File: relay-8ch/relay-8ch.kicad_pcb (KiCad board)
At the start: 2 copper layers, 160 x 100 mm, 49 parts, among them J101 Screw_Terminal_01x16, J201 Backplane, K101 FINDER-40.31, K102 FINDER-40.31, K103 FINDER-40.31, K104 FINDER-40.31, K105 FINDER-40.31, K106 FINDER-40.31, K107 FINDER-40.31, K108 FINDER-40.31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

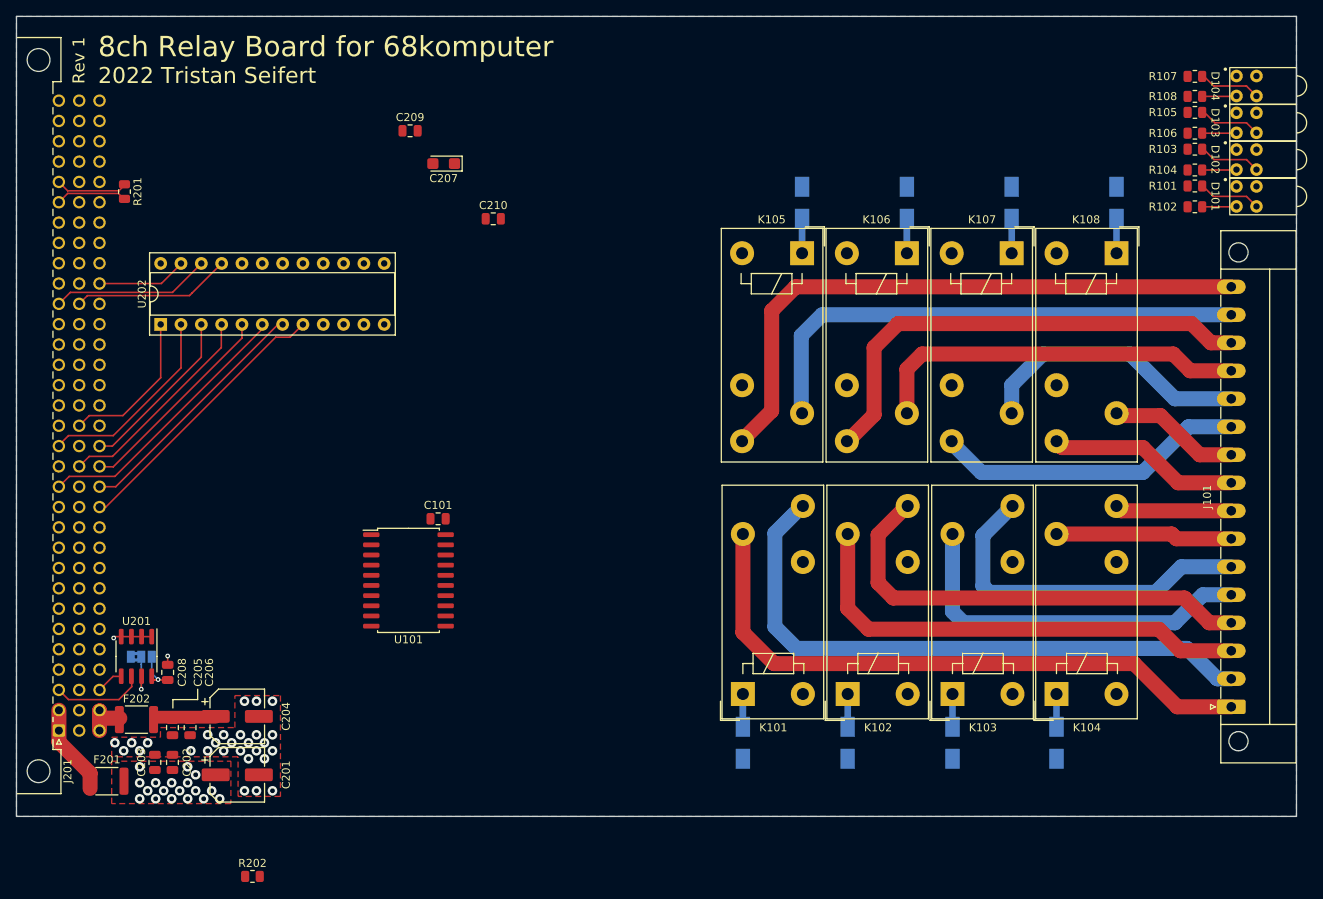
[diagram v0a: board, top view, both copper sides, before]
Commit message: Finished routing relay board
- Completed routing of the relay board; it's got added an address
  selector switch and an I2C expander that can be used to set the
  address automatically.

- Minor tweaks to a few footprints, namely to make sure they're
  correctly tagged as through hole/SMD
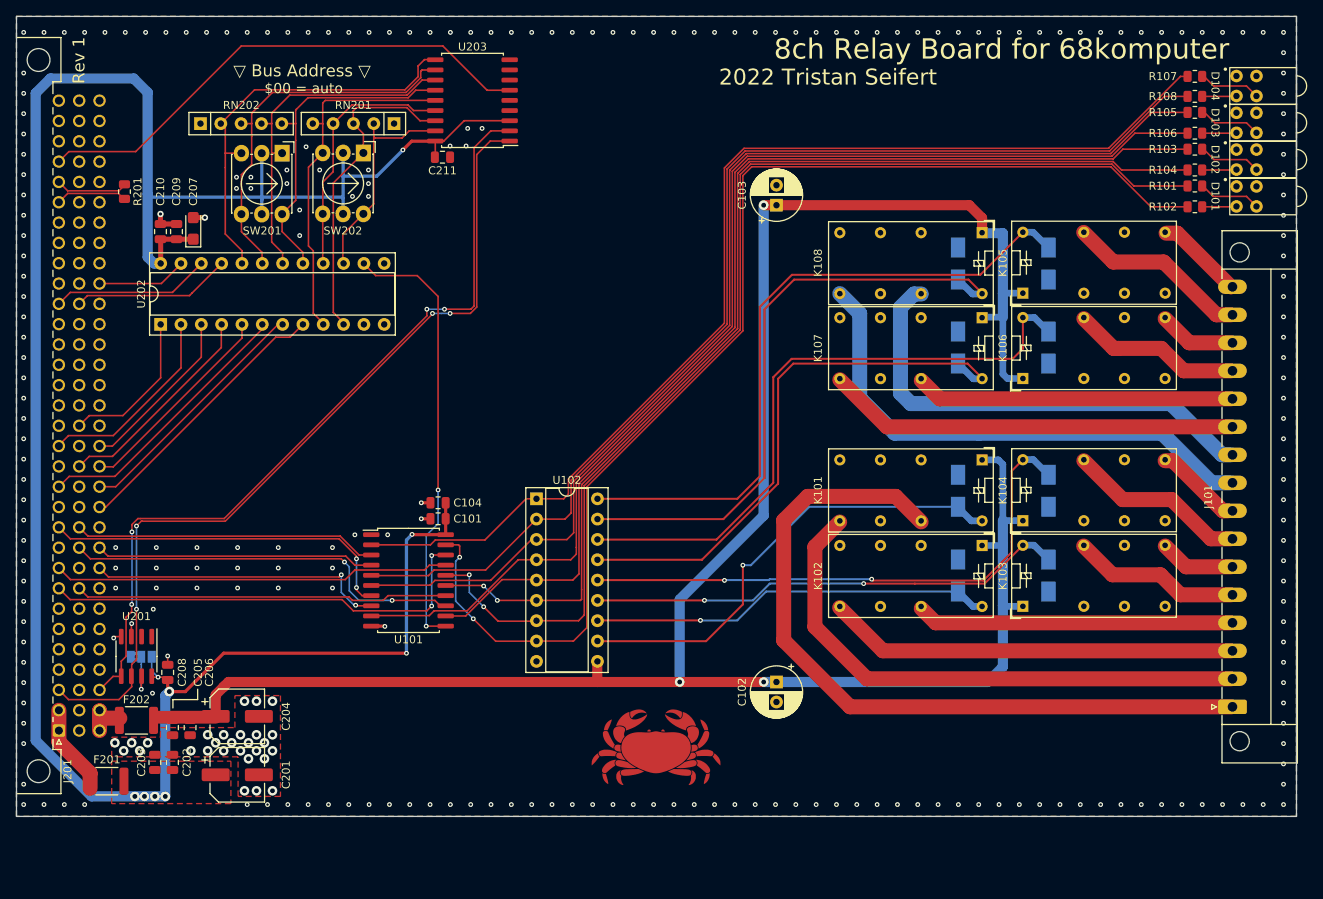
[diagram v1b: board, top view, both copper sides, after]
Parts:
- removed R202: 10k, Resistor_SMD:R_0805_2012Metric
- added C102: 22µF, Capacitor_THT:CP_Radial_D6.3mm_P2.50mm, F.Cu at (115.0, 103.2)
- added C103: 22µF, Capacitor_THT:CP_Radial_D6.3mm_P2.50mm, F.Cu at (115.0, 43.6)
- added C104: 4.7µF, Capacitor_SMD:C_0805_2012Metric, F.Cu at (72.7, 80.8)
- added C211: 100nF, Capacitor_SMD:C_0805_2012Metric, F.Cu at (73.2, 37.6)
- added G***: LOGO, LOGO, F.Cu at (100.0, 111.5)
- added RN201: 10k, Resistor_THT:R_Array_SIP5, F.Cu at (67.2, 33.4)
- added RN202: 10k, Resistor_THT:R_Array_SIP5, F.Cu at (43.0, 33.4)
- added SW201: SW_Coded_SH-7050, Button_Switch_THT:Nidec_Copal_SH-7010C, F.Cu at (53.2, 37.1)
- added SW202: SW_Coded_SH-7050, Button_Switch_THT:Nidec_Copal_SH-7010C, F.Cu at (63.4, 37.1)
- added U102: ULN2803A, Package_DIP:DIP-18_W7.62mm_Socket, F.Cu at (85.0, 80.3)
- added U203: MCP23008-xSO, Package_SO:SOIC-18W_7.5x11.6mm_P1.27mm, F.Cu at (77.0, 30.5)
- K101, K102, K103, K104, K105, K106, K107, K108: value FINDER-40.31 -> G5V-2; footprint Relay_THT:Relay_SPDT_Finder_40.31 -> Relay_THT:Relay_DPDT_Omron_G5V-2
- moved K101 41.8 mm to (140.7, 75.4), turned to -90 degrees
- moved C210 41.6 mm to (38.0, 46.9), turned to 90 degrees
- moved D106 41.4 mm to (137.7, 79.3)
- moved C207 32.3 mm to (42.1, 46.5), turned to 90 degrees
- moved C209 31.8 mm to (40.0, 46.9), turned to 90 degrees
- moved D109 31.7 mm to (149.0, 50.9)
- moved D108 31.5 mm to (149.0, 79.3), turned to 90 degrees
- moved K105 28.0 mm to (145.8, 54.6), turned to 90 degrees
- moved D110 25.3 mm to (149.0, 61.4)
- moved D105 25.0 mm to (137.7, 89.9)
- moved K102 25.0 mm to (140.7, 86.1), turned to -90 degrees
- moved D107 24.1 mm to (149.0, 89.9), turned to 90 degrees
- moved K104 22.1 mm to (145.8, 83.0)
- moved K106 21.3 mm to (145.8, 65.3), turned to 90 degrees
- moved D112 21.2 mm to (137.7, 50.9), turned to -90 degrees
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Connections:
- D105 pad 1: Net-(K102-PadA1) -> GND
- D105 pad 2: GND -> /RELAY1
- D106 pad 1: Net-(K101-PadA1) -> GND
- D106 pad 2: GND -> /RELAY0
- D107 pad 1: Net-(K103-PadA1) -> GND
- D107 pad 2: GND -> /RELAY2
- D108 pad 1: Net-(K104-PadA1) -> GND
- D108 pad 2: GND -> /RELAY3
- D109 pad 1: Net-(K105-PadA1) -> GND
- D109 pad 2: GND -> /RELAY7
- D110 pad 1: Net-(K106-PadA1) -> GND
- D110 pad 2: GND -> /RELAY5
- D111 pad 1: Net-(K107-PadA1) -> GND
- D111 pad 2: GND -> /RELAY4
- D112 pad 1: Net-(K108-PadA1) -> GND
- D112 pad 2: GND -> /RELAY6
- J101 pad 3: /COMM1 -> /SW1
- J101 pad 4: /SW1 -> /COMM1
- J201 pad a11: /Backplane Connection/D2 -> /D2
- J201 pad a8: /Backplane Connection/D7 -> /D7
- J201 pad a9: /Backplane Connection/D6 -> /D6
- J201 pad b10: /Backplane Connection/D4 -> /D4
- J201 pad b11: /Backplane Connection/D0 -> /D0
- J201 pad b8: /Backplane Connection/D5 -> /D5
- J201 pad c10: /Backplane Connection/D1 -> /D1
- J201 pad c9: /Backplane Connection/D3 -> /D3
- K101 pad 11: /COMM0 -> unconnected-(K101-Pad11)
- K102 pad 11: /COMM1 -> unconnected-(K102-Pad11)
- K103 pad 11: /COMM2 -> unconnected-(K103-Pad11)
- K104 pad 11: /COMM3 -> unconnected-(K104-Pad11)
- K105 pad 11: /COMM7 -> unconnected-(K105-Pad11)
- K106 pad 11: /COMM6 -> unconnected-(K106-Pad11)
- K107 pad 11: /COMM5 -> unconnected-(K107-Pad11)
- K108 pad 11: /COMM4 -> unconnected-(K108-Pad11)
- R101 pad 2: unconnected-(R101-Pad2) -> /OUT6
- R102 pad 2: unconnected-(R102-Pad2) -> /OUT7
- R103 pad 2: unconnected-(R103-Pad2) -> /OUT4
- R104 pad 2: unconnected-(R104-Pad2) -> /OUT5
- R105 pad 2: unconnected-(R105-Pad2) -> /OUT2
- R106 pad 2: unconnected-(R106-Pad2) -> /OUT3
- R107 pad 2: unconnected-(R107-Pad2) -> /OUT0
- R108 pad 2: unconnected-(R108-Pad2) -> /OUT1
- U101 pad 12: unconnected-(U101-Pad12) -> /OUT4
- U101 pad 15: unconnected-(U101-Pad15) -> /OUT5
- U101 pad 16: unconnected-(U101-Pad16) -> /OUT6
- U101 pad 19: unconnected-(U101-Pad19) -> /OUT7
- U101 pad 2: unconnected-(U101-Pad2) -> /OUT0
- U101 pad 5: unconnected-(U101-Pad5) -> /OUT1
- U101 pad 6: unconnected-(U101-Pad6) -> /OUT2
- U101 pad 9: unconnected-(U101-Pad9) -> /OUT3
- U202 pad 10: unconnected-(U202-Pad10) -> /Backplane Connection/SET0
- U202 pad 14: /Backplane Connection/LATCH -> /LATCH
- U202 pad 15: unconnected-(U202-Pad15) -> /Backplane Connection/SET3
- U202 pad 16: unconnected-(U202-Pad16) -> /Backplane Connection/SET1
- U202 pad 17: unconnected-(U202-Pad17) -> /Backplane Connection/SET7
- U202 pad 18: unconnected-(U202-Pad18) -> /Backplane Connection/SET4
- U202 pad 19: unconnected-(U202-Pad19) -> /Backplane Connection/SET5
- U202 pad 20: unconnected-(U202-Pad20) -> /Backplane Connection/SET6
- U202 pad 9: unconnected-(U202-Pad9) -> /Backplane Connection/SET2
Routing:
- net +5V: track 5.78 -> 285.8 mm, vias 19 -> 9
- net +12V: track 7.40 -> 270.5 mm, vias 0 -> 3
- net /OUT7: track 0.00 -> 150.9 mm, vias 0 -> 2
- net /OUT3: track 0.00 -> 143.6 mm
- net /OUT6: track 0.00 -> 142.2 mm, vias 0 -> 2
- net /OUT2: track 0.00 -> 141.6 mm
- net /OUT1: track 0.00 -> 140.7 mm
- net /OUT0: track 0.00 -> 138.7 mm
- net /OUT5: track 0.00 -> 136.4 mm, vias 0 -> 2
- net /OUT4: track 0.00 -> 134.9 mm
- net /Backplane Connection/I2C_SDA: track 3.32 -> 102.3 mm, vias 0 -> 4
- net /Backplane Connection/I2C_SCL: track 11.5 -> 108.3 mm, vias 0 -> 4
- net /RELAY7: track 0.00 -> 83.4 mm
- net /RELAY5: track 0.00 -> 78.6 mm
- net /RELAY6: track 0.00 -> 77.3 mm
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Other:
- board text added: "$00 = auto"
- board text added: "▽ Bus Address ▽"

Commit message: Function codes, /DTACK for relay board
- Consider the state of the function code signals (so we don't decode
  CPU space cycles as accesses) and assert /DTACK when the latch signal
  is asserted. This should work for bus speeds of up to around 16MHz
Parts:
- added U204: 74HC00, Package_SO:SOIC-14_3.9x8.7mm_P1.27mm, F.Cu at (40.5, 43.5)
- added U205: 74LVC1G06, 68komputer-common:SC-74-5_1.5x2.9mm_P0.95mm, F.Cu at (34.3, 62.2)
- C207, C209, C210: moved to B.Cu
- moved C207 0.50 mm to (42.1, 47.0)
- moved C209 0.50 mm to (40.0, 47.4)
- moved C210 0.50 mm to (38.0, 47.4)
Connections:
- U202 pad 11: unconnected-(U202-Pad11) -> /Backplane Connection/CPUSPACE
- U202 pad 13: unconnected-(U202-Pad13) -> /Backplane Connection/SET3
- U202 pad 15: /Backplane Connection/SET3 -> unconnected-(U202-Pad15)
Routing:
- net /LATCH: track 55.3 -> 94.8 mm, vias 2 -> 4
- net /Backplane Connection/CPUSPACE: track 0.00 -> 35.8 mm, vias 0 -> 1
- net /Backplane Connection/~{DTACK}: track 0.00 -> 18.8 mm
- net /Backplane Connection/FC1: track 0.00 -> 18.6 mm
- net +5V: track 285.8 -> 301.3 mm, vias 9 -> 11
- net /Backplane Connection/FC0: track 0.00 -> 15.1 mm
- net /Backplane Connection/FC2: track 0.00 -> 9.17 mm
- net GND: track 12.5 -> 7.77 mm, vias 267 -> 291
- net Net-(U204-Pad3): track 0.00 -> 1.28 mm
- net /Backplane Connection/SET3: track 27.2 -> 27.9 mm
- net /SW4: track 64.9 -> 65.5 mm
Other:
- board text added: "0"
- board text added: "1"
- board text added: "1/0"
- board text added: "2"
- board text added: "3"
- board text added: "3/2"
- board text added: "4"
- board text added: "5"
- board text added: "5/4"
- board text added: "6"
- board text added: "7"
- board text added: "7/6"
- board text added: "⚠ 2A/24VDC Max ⚠ ⚠ .6A/115VAC Max ⚠"

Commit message: Tweaks to bill of materials
- Added missing MPN's for a few components; tweaked a few bits of layout
  to increase some tolerances

  This includes kind of tweaking the boot rom socket positions in hopes
  of fitting fancier sockets
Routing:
- net +12V: vias 3 -> 2
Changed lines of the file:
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@@
   (segment (start 44.9 107.5) (end 44.9 104.8) (width 1.27) (layer "F.Cu") (net 3))
   (segment (start 46.5 103.2) (end 92.6 103.2) (width 1.27) (layer "F.Cu") (net 3))
+  (segment (start 92.6 103.2) (end 115 103.2) (width 1.27) (layer "F.Cu") (net 3))
   (segment (start 139.1 43.6) (end 140.7 45.2) (width 1.27) (layer "F.Cu") (net 3))
   (segment (start 44.9 107.6) (end 37.5 107.6) (width 1.6) (layer "F.Cu") (net 3))
-  (segment (start 92.6 103.2) (end 113.4 103.2) (width 1.27) (layer "F.Cu") (net 3))
   (segment (start 44.9 104.8) (end 45.85 103.85) (width 1.27) (layer "F.Cu") (net 3))
   (segment (start 45.85 103.85) (end 46.1 103.6) (width 1.27) (layer "F.Cu") (net 3))
   (segment (start 140.7 45.2) (end 140.7 47) (width 1.27) (layer "F.Cu") (net 3))
   (segment (start 45.85 103.85) (end 46.5 103.2) (width 1.27) (layer "F.Cu") (net 3))
-  (via (at 113.4 103.2) (size 1.2) (drill 0.6) (layers "F.Cu" "B.Cu") (net 3))
   (via (at 102.9 103.2) (size 1.2) (drill 0.6) (layers "F.Cu" "B.Cu") (net 3))
   (via (at 113.4 43.6) (size 1.2) (drill 0.6) (layers "F.Cu" "B.Cu") (net 3))
@@
   (segment (start 143.3 76) (end 143.3 83) (width 0.8382) (layer "B.Cu") (net 3))
   (segment (start 143.8625 65.2625) (end 143.3 64.7) (width 0.8382) (layer "B.Cu") (net 3))
-  (segment (start 113.4 103.2) (end 141.4 103.2) (width 1.27) (layer "B.Cu") (net 3))
-  (segment (start 143.3 101.3) (end 143.3 96.4) (width 1.27) (layer "B.Cu") (net 3))
   (segment (start 143.3 86.1) (end 143.3 93.6) (width 1.27) (layer "B.Cu") (net 3))
   (segment (start 143.3 83) (end 143.3 86.1) (width 1.27) (layer "B.Cu") (net 3))
   (segment (start 145.8 65.2625) (end 143.8625 65.2625) (width 0.8382) (layer "B.Cu") (net 3))
+  (segment (start 115 103.2) (end 141.4 103.2) (width 1.27) (layer "B.Cu") (net 3))
+  (segment (start 143.3 101.3) (end 143.3 93.6) (width 1.27) (layer "B.Cu") (net 3))
   (segment (start 143.3 64.7) (end 143.3 57.6) (width 0.8382) (layer "B.Cu") (net 3))
-  (segment (start 143.3 93.6) (end 143.3 96.4) (width 1.27) (layer "B.Cu") (net 3))
   (segment (start 143.3 57.6) (end 143.3 54.6) (width 1.27) (layer "B.Cu") (net 3))
   (segment (start 140.7 86.1375) (end 143.2625 86.1375) (width 0.8382) (layer "B.Cu") (net 3))
+  (segment (start 141.4 103.2) (end 143.3 101.3) (width 1.27) (layer "B.Cu") (net 3))
   (segment (start 143.3 57.6) (end 140.7 57.6) (width 0.8382) (layer "B.Cu") (net 3))
   (segment (start 113.4 43.6) (end 113.4 82.4) (width 1.27) (layer "B.Cu") (net 3))
@@
   (segment (start 102.9 92.9) (end 102.9 103.2) (width 1.27) (layer "B.Cu") (net 3))
   (segment (start 143.2625 86.1375) (end 143.3 86.1) (width 0.8382) (layer "B.Cu") (net 3))
-  (segment (start 141.4 103.2) (end 143.3 101.3) (width 1.27) (layer "B.Cu") (net 3))
   (segment (start 25.3 106.73) (end 25.3 110.7) (width 1.8796) (layer "F.Cu") (net 4))
   (segment (start 25.3 110.7) (end 29.2 114.6) (width 1.8796) (layer "F.Cu") (net 4))

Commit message: Switched remaining pluggable screw terminals
- Replaced the pluggable/replaceable screw terminals with CUI devices
  parts on the backplane (+12V/GND/+5V) and relay board (switched
  contacts) since they're much cheaper and basically the same thing as
  the corresponding WE/Phoenix Contact parts
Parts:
- J101: footprint Connector_Phoenix_MC:PhoenixContact_MC_1,5_16-GF-3.5_1x16_P3.50mm_Horizontal_ThreadedFlange_MountHole -> 68komputer-common:CUI_TBP02R1W-381-16BE
- moved J101 55.5 mm to (172.0, 50.8), turned to -90 degrees
- moved R101 2.05 mm to (167.3, 39.1)
- moved R103 2.05 mm to (167.3, 34.5)
- moved R104 2.05 mm to (167.3, 37.1)
- moved R106 2.05 mm to (167.3, 32.5)
- moved D104 2.05 mm to (180.0, 26.6)
- moved R105 2.05 mm to (167.3, 29.9)
- moved R107 2.05 mm to (167.3, 25.4)
- moved R108 2.05 mm to (167.3, 27.9)
- moved D101 2.05 mm to (180.0, 40.5)
- moved D102 2.05 mm to (180.0, 35.9)
- moved D103 2.05 mm to (180.0, 31.2)
- moved R102 2.05 mm to (167.3, 41.8)
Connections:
- J101 pad 1: /COMM0 -> /SW7
- J101 pad 10: /COMM4 -> /COMM3
- J101 pad 11: /SW5 -> /SW2
- J101 pad 12: /COMM5 -> /COMM2
- J101 pad 13: /COMM6 -> /COMM1
- J101 pad 14: /SW6 -> /SW1
- J101 pad 15: /COMM7 -> /SW0
- J101 pad 16: /SW7 -> /COMM0
- J101 pad 2: /SW0 -> /COMM7
- J101 pad 3: /SW1 -> /SW6
- J101 pad 4: /COMM1 -> /COMM6
- J101 pad 5: /COMM2 -> /COMM5
- J101 pad 6: /SW2 -> /SW5
- J101 pad 7: /COMM3 -> /COMM4
- J101 pad 8: /SW3 -> /SW4
- J101 pad 9: /SW4 -> /SW3
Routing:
- net /SW7: track 10.9 -> 9.79 mm
- net +12V: track 270.5 -> 269.5 mm, vias 2 -> 1
- net /COMM5: track 39.7 -> 40.6 mm
- net /SW6: track 9.57 -> 8.68 mm
- net /COMM7: track 22.7 -> 21.8 mm
- net /OUT2: track 141.6 -> 142.4 mm
- net /OUT5: track 136.4 -> 137.3 mm
- net /OUT7: track 150.9 -> 151.7 mm
- net /OUT4: track 134.9 -> 135.8 mm
- net /OUT0: track 138.7 -> 139.6 mm
- net /OUT6: track 142.2 -> 143.0 mm
- net /OUT3: track 143.6 -> 144.4 mm
- net /OUT1: track 140.7 -> 141.5 mm
- net /COMM0: track 94.2 -> 94.9 mm
- net /SW5: track 51.4 -> 52.1 mm
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
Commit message: Removed GAL from relay board
- Replaced the GAL on the relay board with some hard 74-series logic;
  this means the board needs zero "hard to get" parts.

  All the address decoding is done by a '688 magnitude comparison IC,
  which is LS logic so this board needs to consist of HCT logic to deal
  with its lower active high level.

- Replaced 3D model for the hexadecimal rotary switches to one that has
  color :D
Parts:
- added C212: 100nF, Capacitor_SMD:C_0805_2012Metric, F.Cu at (34.1, 65.0)
- added C213: 100nF, Capacitor_SMD:C_0805_2012Metric, F.Cu at (64.3, 51.6)
- added C214: 100nF, Capacitor_SMD:C_0805_2012Metric, F.Cu at (68.9, 56.6)
- added U206: 74HCT32, Package_SO:SO-14_3.9x8.65mm_P1.27mm, F.Cu at (62.8, 57.2)
- added U207: 74LS688, Package_SO:SOIC-20W_7.5x12.8mm_P1.27mm, F.Cu at (48.5, 59.0)
- C207, C210: moved to F.Cu
- C209: value 4.7µF -> 100nF; moved to F.Cu
- U202: value ATF22V10C -> 74HCT1G04G; footprint Package_DIP:DIP-24_W7.62mm_Socket -> 68komputer-common:SC-74-5_1.5x2.9mm_P0.95mm
- U204: value 74HC00 -> 74HCT08; footprint Package_SO:SOIC-14_3.9x8.7mm_P1.27mm -> Package_SO:SO-14_3.9x8.65mm_P1.27mm
- moved U202 30.9 mm to (68.9, 59.8)
- moved C207 21.9 mm to (63.9, 49.5), turned to 180 degrees
- moved C209 16.7 mm to (55.9, 52.5)
- moved C210 10.3 mm to (42.0, 37.9), turned to 180 degrees
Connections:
- U202 pad 1: /Backplane Connection/A16 -> (no net)
- U202 pad 2: /Backplane Connection/A20 -> /Backplane Connection/~{LATCH}
- U202 pad 3: /Backplane Connection/A18 -> GND
- U202 pad 4: /Backplane Connection/A21 -> /LATCH
- U202 pad 5: /Backplane Connection/A17 -> +5V
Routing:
- net +5V: track 301.3 -> 347.0 mm, vias 11 -> 15
- net /Backplane Connection/SET3: track 27.9 -> 56.1 mm, vias 0 -> 2
- net /Backplane Connection/SET1: track 32.2 -> 54.2 mm, vias 0 -> 2
- net /Backplane Connection/R/~{W}: track 19.7 -> 38.3 mm, vias 0 -> 1
- net /LATCH: track 94.8 -> 79.3 mm, vias 4 -> 5
- net /Backplane Connection/SET4: track 44.1 -> 58.4 mm
- net /Backplane Connection/SET0: track 40.3 -> 54.4 mm, vias 0 -> 2
- net /Backplane Connection/SET2: track 44.6 -> 58.5 mm, vias 0 -> 2
- net /Backplane Connection/A23: track 34.2 -> 47.3 mm, vias 0 -> 1
- net /Backplane Connection/~{LDS}: track 19.9 -> 33.0 mm, vias 0 -> 1
- net /Backplane Connection/SET5: track 47.4 -> 60.2 mm, vias 0 -> 2
- net /Backplane Connection/SET6: track 51.5 -> 62.9 mm, vias 0 -> 2
- net /Backplane Connection/A21: track 26.7 -> 36.4 mm, vias 0 -> 1
- net /Backplane Connection/A16: track 19.3 -> 28.4 mm
- net /Backplane Connection/SET7: track 41.2 -> 48.7 mm
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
